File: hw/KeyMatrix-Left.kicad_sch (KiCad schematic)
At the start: 116 parts, among them SW3300 SW_Cherry_MX_RGB, SW3301 SW_Cherry_MX_RGB, SW3302 SW_Cherry_MX_RGB, SW3303 SW_Cherry_MX_RGB, SW3304 SW_Cherry_MX_RGB, SW3305 SW_Cherry_MX_RGB, SW3306 SW_Cherry_MX_RGB, SW3307 SW_Cherry_MX_RGB, SW3308 SW_Cherry_MX_RGB, SW3309 SW_Cherry_MX_RGB, SW3310 SW_Cherry_MX_RGB, SW3311 SW_Cherry_MX_RGB, SW3312 SW_Cherry_MX_RGB, SW3313 SW_Cherry_MX_RGB, SW3314 SW_Cherry_MX_RGB, SW3315 SW_Cherry_MX_RGB, SW3316 SW_Cherry_MX_RGB, SW3317 SW_Cherry_MX_RGB, SW3318 SW_Cherry_MX_RGB, SW3319 SW_Cherry_MX_RGB, SW3320 SW_Cherry_MX_RGB, SW3321 SW_Cherry_MX_RGB, SW3322 SW_Cherry_MX_RGB, SW3323 SW_Cherry_MX_RGB, SW3324 SW_Cherry_MX_RGB, SW3325 SW_Cherry_MX_RGB, SW3326 SW_Cherry_MX_RGB, SW3327 SW_Cherry_MX_RGB, SW3328 SW_Cherry_MX_RGB, SW3329 SW_Cherry_MX_RGB, SW3330 SW_Cherry_MX_RGB, SW3331 SW_Cherry_MX_RGB, SW3332 SW_Cherry_MX_RGB, SW3333 SW_Cherry_MX_RGB, SW3334 SW_Cherry_MX_RGB, SW3335 SW_Cherry_MX_RGB, X3300 Keycap-R1-1x1, X3301 Keycap-R1-1x1, X3302 Keycap-R1-1x1, X3303 Keycap-R1-1x1, X3304 Keycap-R1-1x1, X3305 Keycap-R1-1x1, X3306 Keycap-R1-1x1, X3307 Keycap-R1-1x1, X3308 Keycap-R1-1x1, X3309 Keycap-R1-1x1, X3310 Keycap-R1-1x1, X3311 Keycap-R1-1x1, X3312 Keycap-R1-1x1, X3313 Keycap-R1-1.5x1, X3314 Keycap-R1-1x1, X3315 Keycap-R1-1x1, X3316 Keycap-R1-1x1, X3317 Keycap-R1-1x1, X3318 Keycap-R1-1x1, X3319 Keycap-R1-1.75x1, X3320 Keycap-R1-1x1, X3321 Keycap-R1-1x1, X3322 Keycap-R1-1x1, X3323 Keycap-R1-1x1, X3324 Keycap-R1-1x1, X3325 Keycap-R1-2x1, X3326 Keycap-R1-1.25x1, X3327 Keycap-R1-1x1, X3328 Keycap-R1-1x1, X3329 Keycap-R1-1x1, X3330 Keycap-R1-1x1, X3331 Keycap-R1-1x1, X3332 Keycap-R1-1.25x1, X3333 Keycap-R1-1.25x1, X3334 Keycap-R1-1.25x1, X3335 Keycap-R1-2.75x1, X3336 STAB-0G990224, X3337 STAB-0G990224

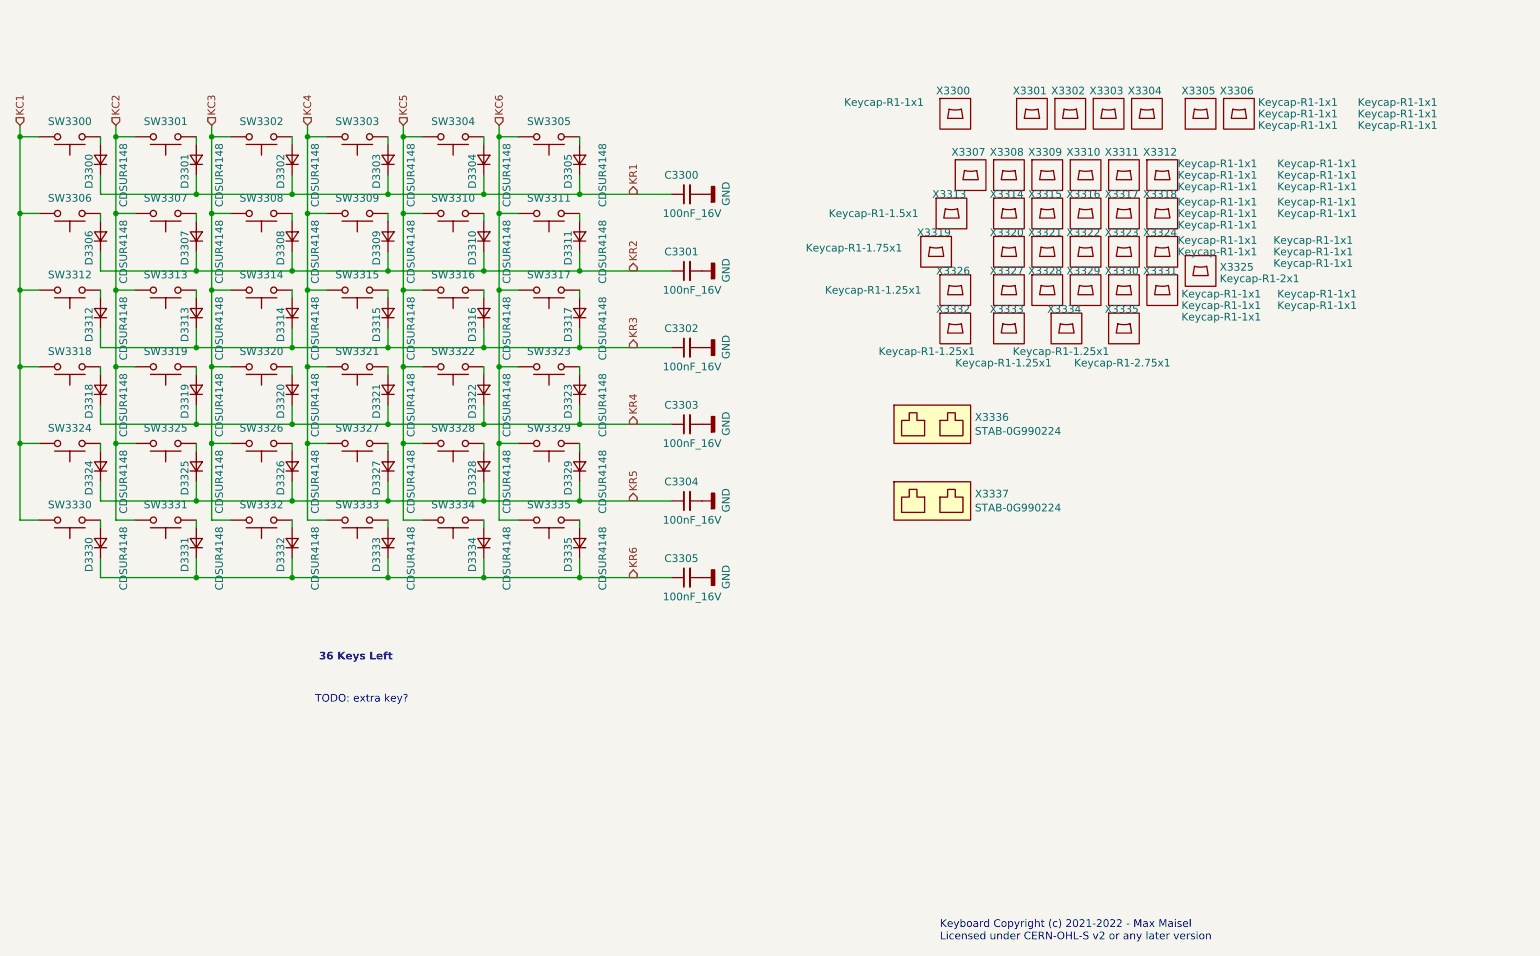
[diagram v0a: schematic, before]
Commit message: Add ESD diodes to key matrix pins.
Better save than sorry.
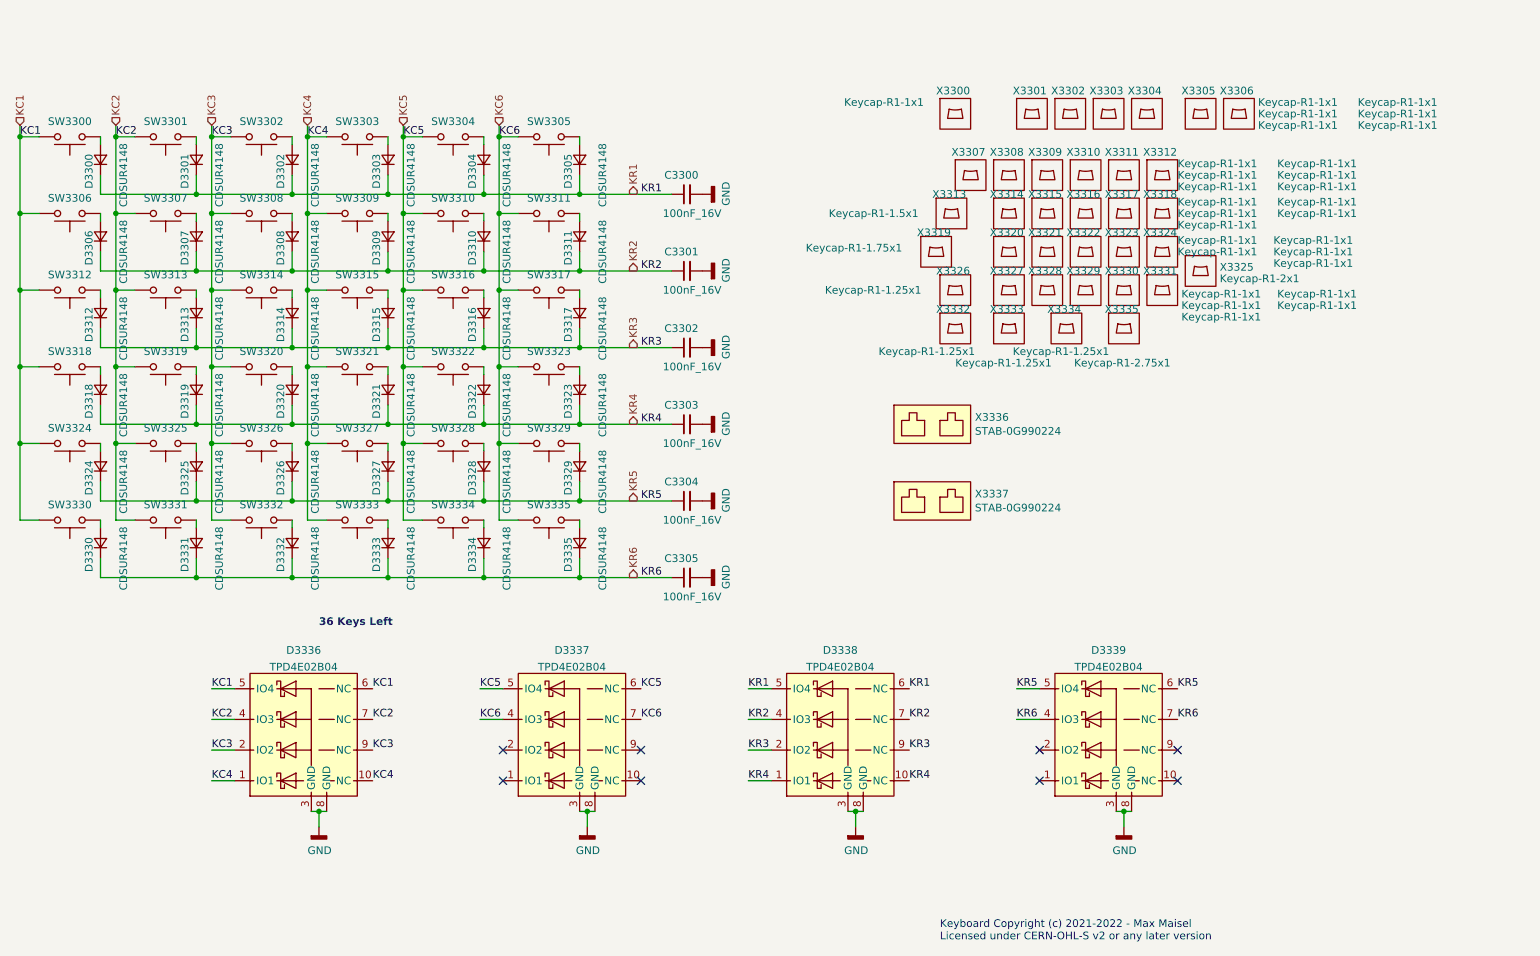
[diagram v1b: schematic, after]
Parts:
- added D3336, D3337, D3338, D3339: TPD4E02B04, Keyboard:USON10, symbol Keyboard:TPD4E02B04
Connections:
- net GND: now also D3336.3 (GND), D3336.8 (GND), D3337.3 (GND), D3337.8 (GND), D3338.3 (GND), D3338.8 (GND), D3339.3 (GND), D3339.8 (GND)
- net KC1: now also D3336.5 (IO4), D3336.6 (NC)
- net KC2: now also D3336.4 (IO3), D3336.7 (NC)
- net KC3: now also D3336.2 (IO2), D3336.9 (NC)
- net KC4: now also D3336.1 (IO1), D3336.10 (NC)
- net KC5: now also D3337.5 (IO4), D3337.6 (NC)
- net KC6: now also D3337.4 (IO3), D3337.7 (NC)
- net KR1: now also D3338.5 (IO4), D3338.6 (NC)
- net KR2: now also D3338.4 (IO3), D3338.7 (NC)
- net KR3: now also D3338.2 (IO2), D3338.9 (NC)
- net KR4: now also D3338.1 (IO1), D3338.10 (NC)
- net KR5: now also D3339.5 (IO4), D3339.6 (NC)
- net KR6: now also D3339.4 (IO3), D3339.7 (NC)
- no-connect marks 0 -> 8
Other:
- note removed: "TODO: extra key?"

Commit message: Update schematic:
- Add ESD protection.
- Adjust distance bolts so they fit to the MX mounting plate.
- Make key layout symmetric.
- Add resistor to TX driver outputs.
- Use alternate IO functions on inter-board connectors.
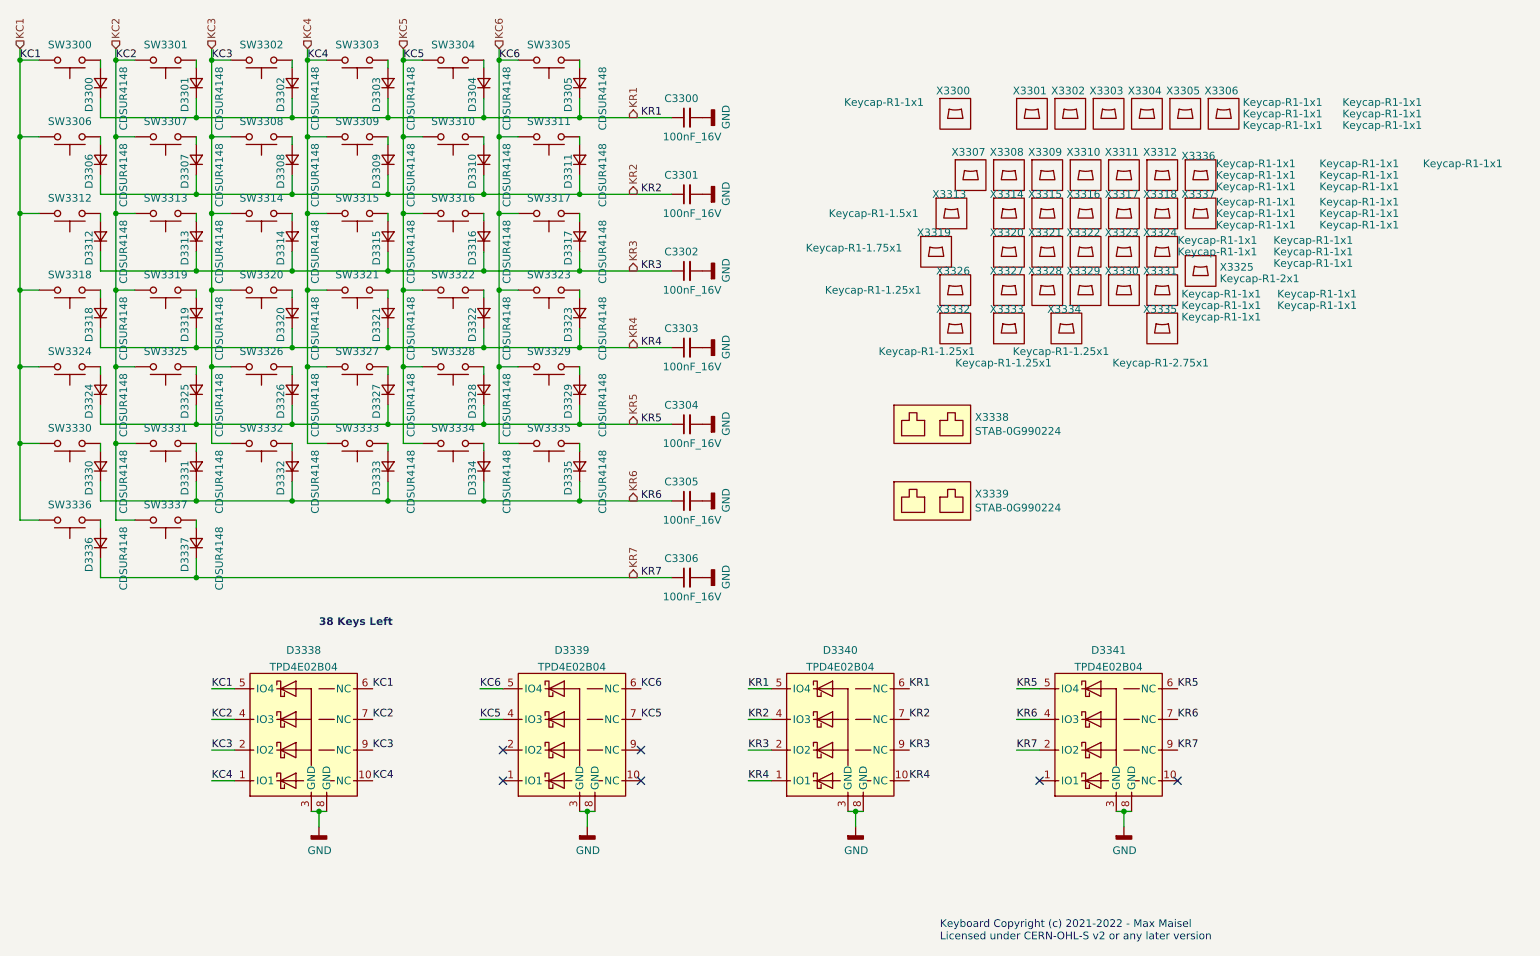
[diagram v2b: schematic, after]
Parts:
- added C3306: 100nF_16V, Keyboard:C_0402, symbol Keyboard:100nF_16V
- added D3336, D3337: CDSUR4148, Keyboard:SOD-523, symbol Keyboard:CDSUR4148
- added SW3336, SW3337: SW_Cherry_MX_RGB, Keyboard:SW_Cherry_MX1A_RGB, symbol Keyboard:SW_Cherry_MX_RGB
- added X3336, X3337: Keycap-R1-1x1, Keyboard:Keycap-R1-1x1, symbol Keyboard:Keycap-R1-1x1
- renumbered D3336 to D3338, D3337 to D3339, D3338 to D3340, D3339 to D3341, X3336 to X3338, X3337 to X3339
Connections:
- net GND: now also C3306.2
- net KC1: now also SW3336.1
- net KC2: now also SW3337.1
- net KC5: now also D3339.4 (IO3), D3339.7 (NC); no longer D3339.5 (IO4), D3339.6 (NC)
- net KC6: now also D3339.5 (IO4), D3339.6 (NC); no longer D3339.4 (IO3), D3339.7 (NC)
- net KR7: now reaches D3341.2 (IO2)
- net KR7: now also D3341.9 (NC), C3306.1, D3336.1 (K), D3337.1 (K)
- new net: D3336.2 (A), SW3336.2
- new net: D3337.2 (A), SW3337.2
- no-connect marks 8 -> 6
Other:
- note added: "38 Keys Left"
- note removed: "36 Keys Left"
- moved on the sheet: C3300, C3301, C3302, C3303, C3304, C3305, D3300, D3301, D3302, D3303, D3304, D3305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

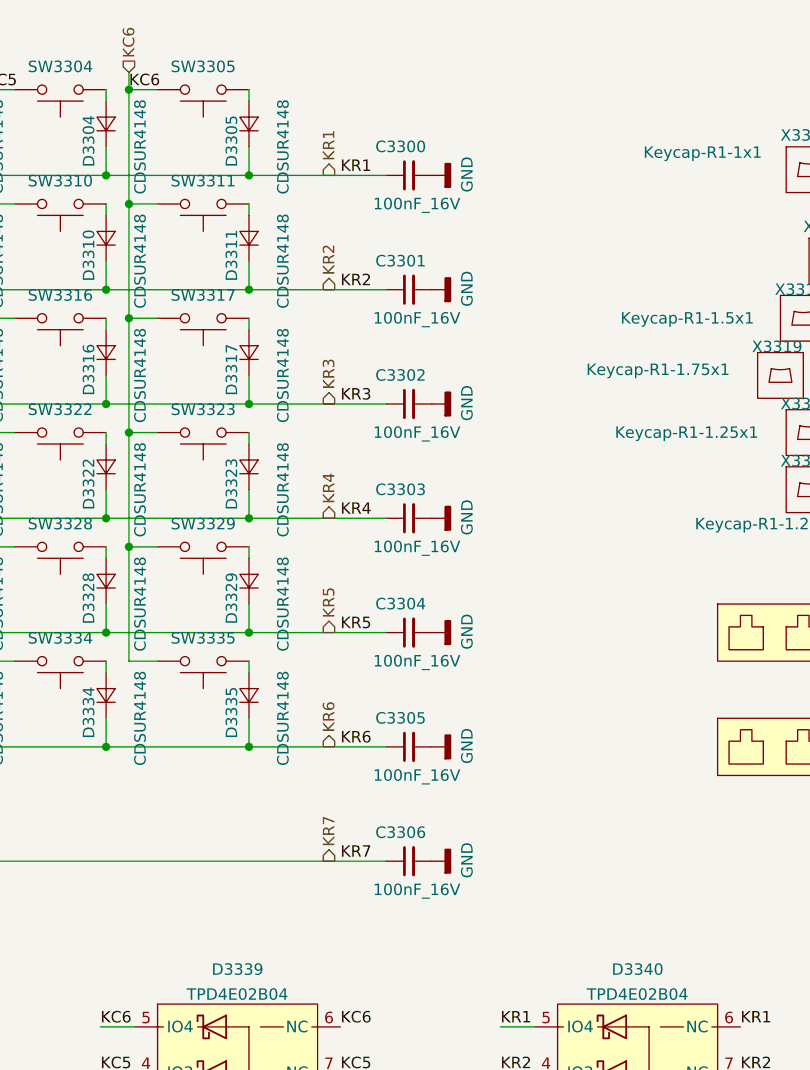
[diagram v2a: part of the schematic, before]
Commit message: Change key matrix capacitors to 220pF.
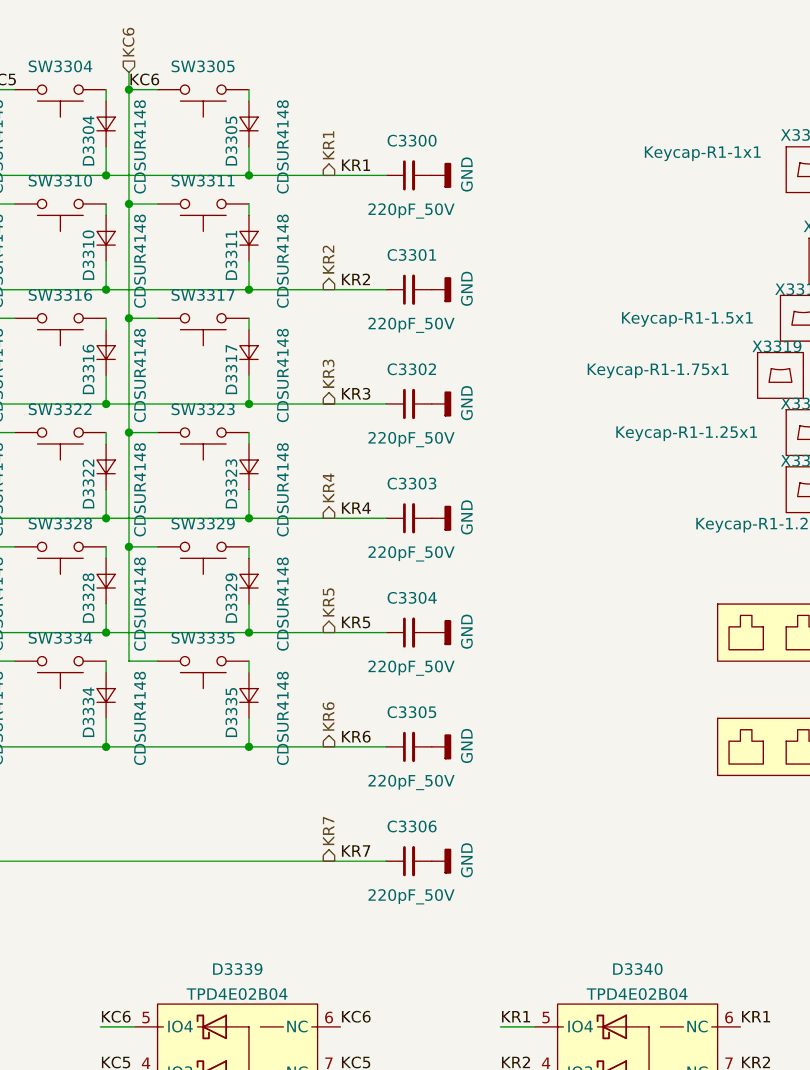
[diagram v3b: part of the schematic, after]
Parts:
- removed C3300, C3301, C3302, C3303, C3304, C3305, C3306: 100nF_16V, Keyboard:C_0402, symbol Keyboard:100nF_16V
- added C3300, C3301, C3302, C3303, C3304, C3305, C3306: 220pF_50V, Keyboard:C_0402, symbol Keyboard:220pF_50V
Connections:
- net GND: now also C3300.2, C3301.2, C3302.2, C3303.2, C3304.2, C3305.2, C3306.2
- net KR1: now also C3300.1
- net KR2: now also C3301.1
- net KR3: now also C3302.1
- net KR4: now also C3303.1
- net KR5: now also C3304.1
- net KR6: now also C3305.1
- net KR7: now also C3306.1
